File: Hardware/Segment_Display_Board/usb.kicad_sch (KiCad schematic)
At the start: 12 parts, among them J301 USB_B_Micro, J302 PROG, U301 FT232RL

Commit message: Fix stuff i guess goodnight"
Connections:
- net +3V3 renamed +3.3V
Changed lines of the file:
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@@
     (title "Days Without Incident Sign")
     (date "2022-06-24")
-    (rev "v0.1-RC1")
+    (rev "${REVISION}")
     (company "FRC 1721")
+    (comment 4 "Release: ${FULL_REVISION}")
   )
   (junction (at 105.41 76.2) (diameter 0) (color 0 0 0 0)

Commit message: include fixups fro EE
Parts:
- removed C302: 4.7uf, Capacitor_SMD:CP_Elec_4x3, symbol Device:C_Polarized_Small
- added C302: 100nF, Capacitor_SMD:C_0805_2012Metric, symbol Device:C_Small
- added R301: 4K7, Resistor_SMD:R_0805_2012Metric, symbol Device:R_Small
- added R302: 10K, Resistor_SMD:R_0805_2012Metric, symbol Device:R_Small
- C303: value 100nf -> 100nF
- renumbered R301 to R303, R302 to R304
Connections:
- net +5V: now also C303.1, C302.1
- net GND: now also C302.2, R302.1
- net VBUS: now also R301.2; no longer C303.1
- net at U301.19 (~{RESET}): now also R301.1, R302.2
- no-connect marks 14 -> 13
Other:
- note added: "Crystal here"
- moved on the sheet: C301, J301

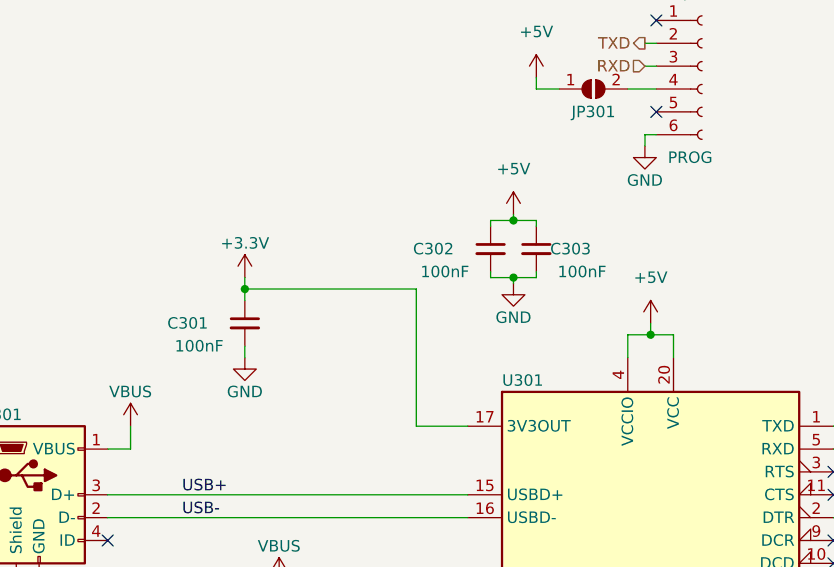
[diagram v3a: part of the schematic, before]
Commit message: Add breakout for external buttons
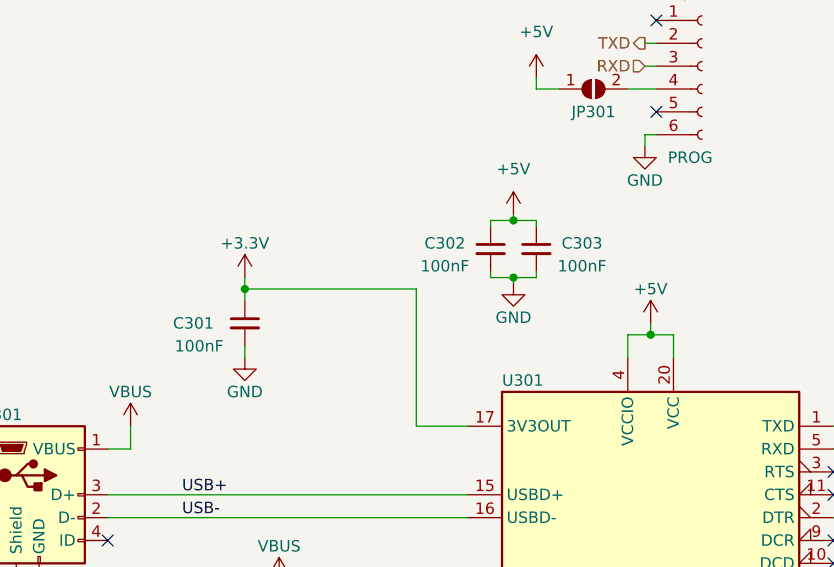
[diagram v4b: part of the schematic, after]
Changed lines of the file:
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@@
   )
   (symbol (lib_id "power:+5V") (at 144.78 64.77 0) (unit 1)
-    (in_bom yes) (on_board yes) (fields_autoplaced)
+    (in_bom yes) (on_board yes)
     (property "Reference" "#PWR0313" (id 0) (at 144.78 68.58 0)
       (effects (font (size 1.27 1.27)) hide)
     )
-    (property "Value" "+5V" (id 1) (at 144.78 59.69 0))
+    (property "Value" "+5V" (id 1) (at 144.78 60.96 0))
     (property "Footprint" "" (id 2) (at 144.78 64.77 0)
       (effects (font (size 1.27 1.27)) hide)
@@
   (symbol (lib_id "Device:C_Small") (at 127 56.515 0) (unit 1)
     (in_bom yes) (on_board yes)
-    (property "Reference" "C302" (id 0) (at 120.65 56.515 0))
-    (property "Value" "100nF" (id 1) (at 121.92 59.055 0))
+    (property "Reference" "C302" (id 0) (at 121.92 55.88 0))
+    (property "Value" "100nF" (id 1) (at 121.92 58.42 0))
     (property "Footprint" "Capacitor_SMD:C_0805_2012Metric" (id 2) (at 127 56.515 0)
       (effects (font (size 1.27 1.27)) hide)
@@
   (symbol (lib_id "Device:C_Small") (at 99.695 64.77 0) (unit 1)
     (in_bom yes) (on_board yes)
-    (property "Reference" "C301" (id 0) (at 93.345 64.77 0))
+    (property "Reference" "C301" (id 0) (at 93.98 64.77 0))
     (property "Value" "100nF" (id 1) (at 94.615 67.31 0))
     (property "Footprint" "Capacitor_SMD:C_0805_2012Metric" (id 2) (at 99.695 64.77 0)
@@
   (symbol (lib_id "Device:C_Small") (at 132.08 56.515 0) (unit 1)
     (in_bom yes) (on_board yes)
-    (property "Reference" "C303" (id 0) (at 135.89 56.515 0))
-    (property "Value" "100nF" (id 1) (at 137.16 59.055 0))
+    (property "Reference" "C303" (id 0) (at 137.16 55.88 0))
+    (property "Value" "100nF" (id 1) (at 137.16 58.42 0))
     (property "Footprint" "Capacitor_SMD:C_0805_2012Metric" (id 2) (at 132.08 56.515 0)
       (effects (font (size 1.27 1.27)) hide)
